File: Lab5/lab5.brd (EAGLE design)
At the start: 106 x 106 mm, 56 parts, among them J1 ISP, Q1 SI2302CDS, Q2 SI2302CDS, Q3 SI2302CDS, Q4 SI2302CDS, U1 ATMEGA128RFA1, Y1 16MHz

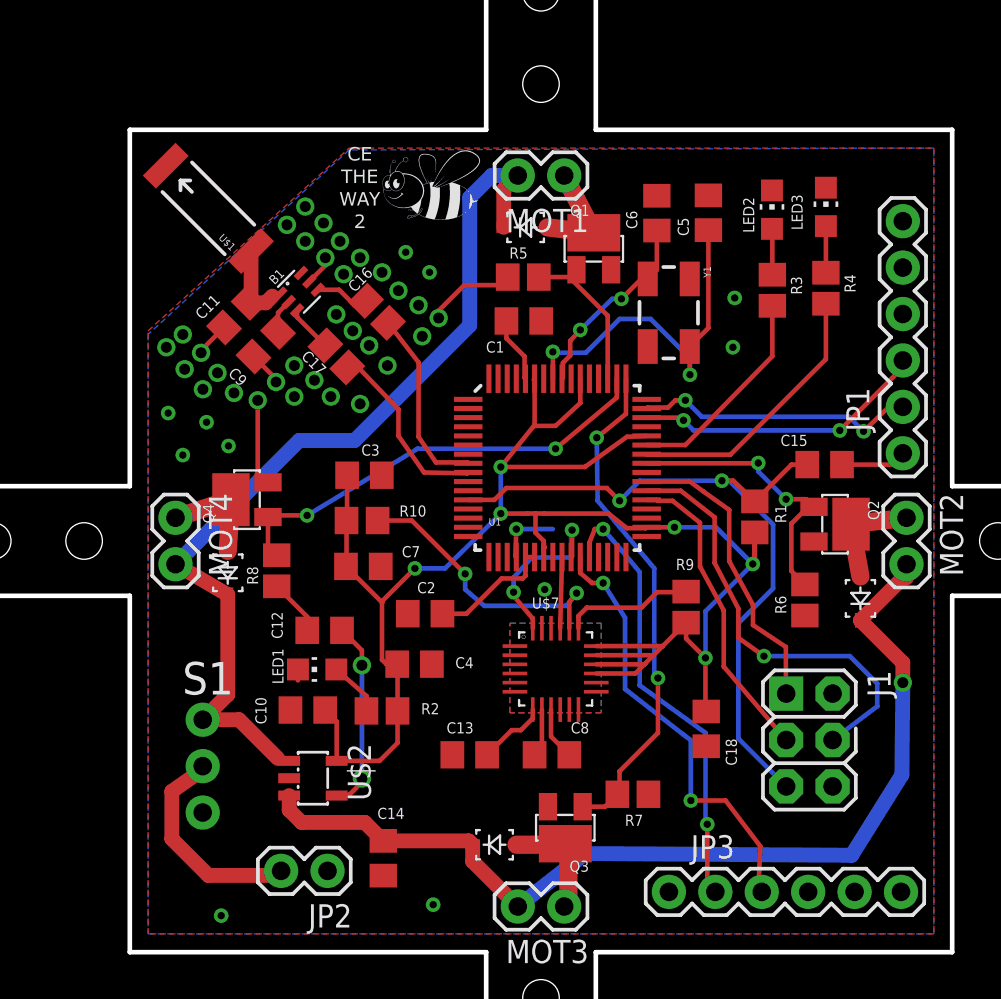
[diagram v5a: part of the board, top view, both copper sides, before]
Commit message: Added Some Restrict Around IMU
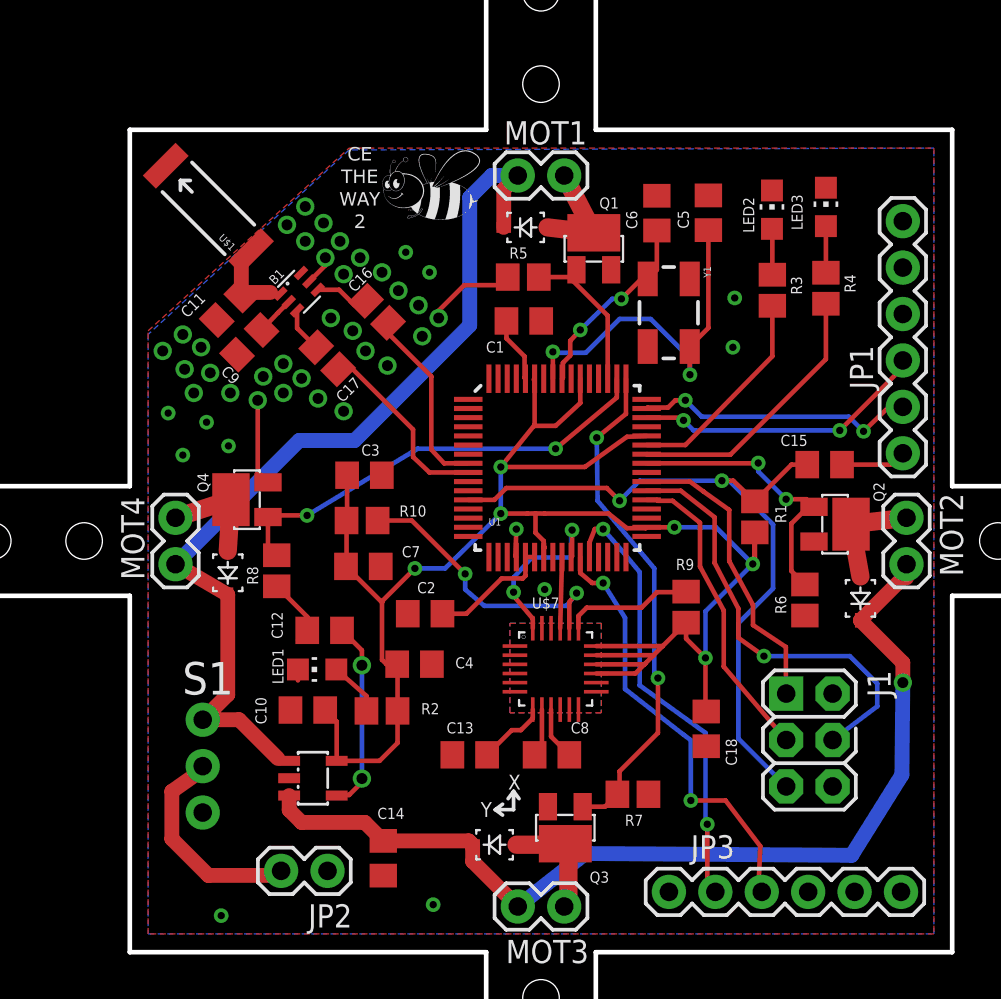
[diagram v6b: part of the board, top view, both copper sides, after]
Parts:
- moved C11 0.91 mm to (-16.0, 10.9)
- moved C9 0.57 mm to (-17.1, 12.8)
- moved C17 0.51 mm to (-11.7, 10.0)
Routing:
- net GND: track 23.2 -> 17.4 mm
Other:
- board text added: "X"
- board text added: "Y"
